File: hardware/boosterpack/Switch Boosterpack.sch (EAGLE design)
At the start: 36 parts, among them IC1 LAUNCHPAD-50MM, Q1 IRFR3709, Q2 IRFR3709, Q3 IRFR3709, Q4 IRFR3709

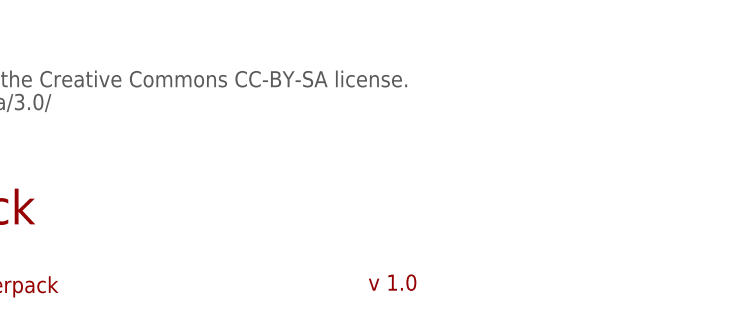
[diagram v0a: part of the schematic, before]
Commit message: Tweaked silkscreen and made OLED ribbon cutoff longer.
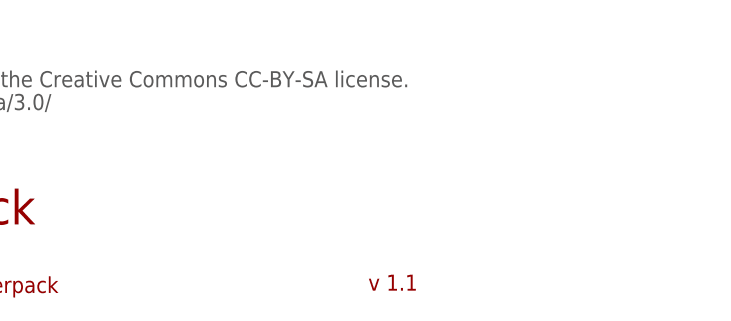
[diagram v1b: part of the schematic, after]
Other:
- note added: "v 1.1"
- note removed: "v 1.0"
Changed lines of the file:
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@@
 <?xml version="1.0" encoding="utf-8"?>
 <!DOCTYPE eagle SYSTEM "eagle.dtd">
-<eagle version="6.2">
+<eagle version="6.3">
 <drawing>
 <settings>
@@
 <layers>
 <layer number="1" name="Top" color="4" fill="1" visible="no" active="no"/>
+<layer number="2" name="Route2" color="1" fill="3" visible="no" active="no"/>
+<layer number="15" name="Route15" color="4" fill="6" visible="no" active="no"/>
 <layer number="16" name="Bottom" color="1" fill="1" visible="no" active="no"/>
 <layer number="17" name="Pads" color="2" fill="1" visible="no" active="no"/>
@@
 <text x="292.1" y="12.7" size="3.81" layer="94">Switch Boosterpack</text>
 <text x="290.83" y="5.08" size="1.778" layer="94">www.github.com/andresv/switch-boosterpack</text>
-<text x="375.412" y="5.334" size="1.778" layer="94">v 1.0</text>
+<text x="375.412" y="5.334" size="1.778" layer="94">v 1.1</text>
 <text x="288.29" y="27.94" size="1.778" layer="97">This work is licensed under version 3.0 of the Creative Commons CC-BY-SA license.</text>
 <text x="288.29" y="25.4" size="1.778" layer="97">http://creativecommons.org/licenses/by-sa/3.0/</text>

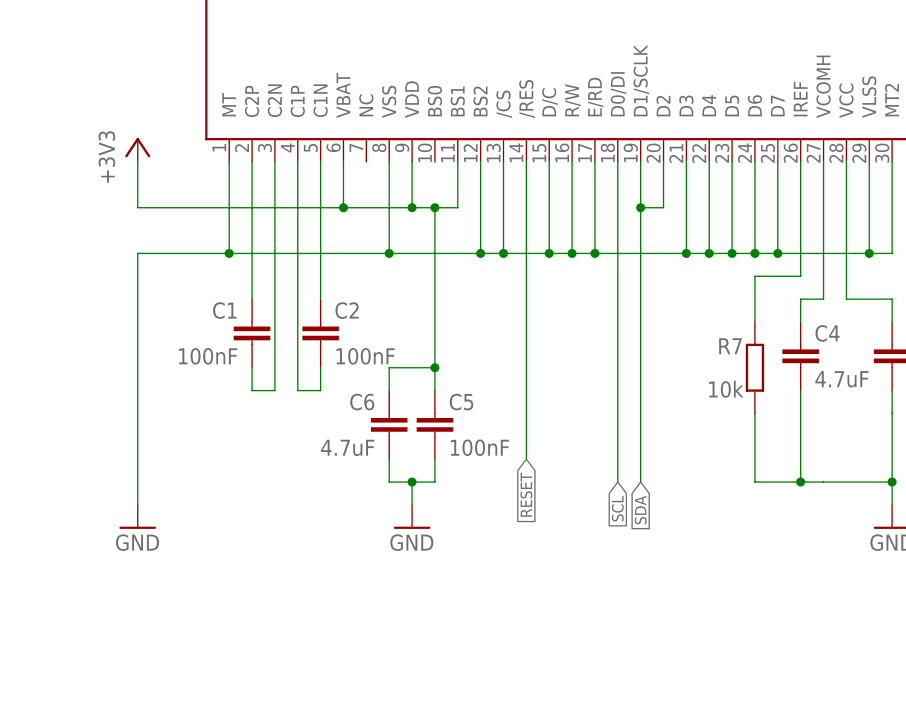
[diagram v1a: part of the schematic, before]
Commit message: BS0 is now tied to GND, C1, C2 are 1 uF and R7 is 390k.
Those are main v1.0 errors. They must be fixed otherwise v1.0 boards are not working.
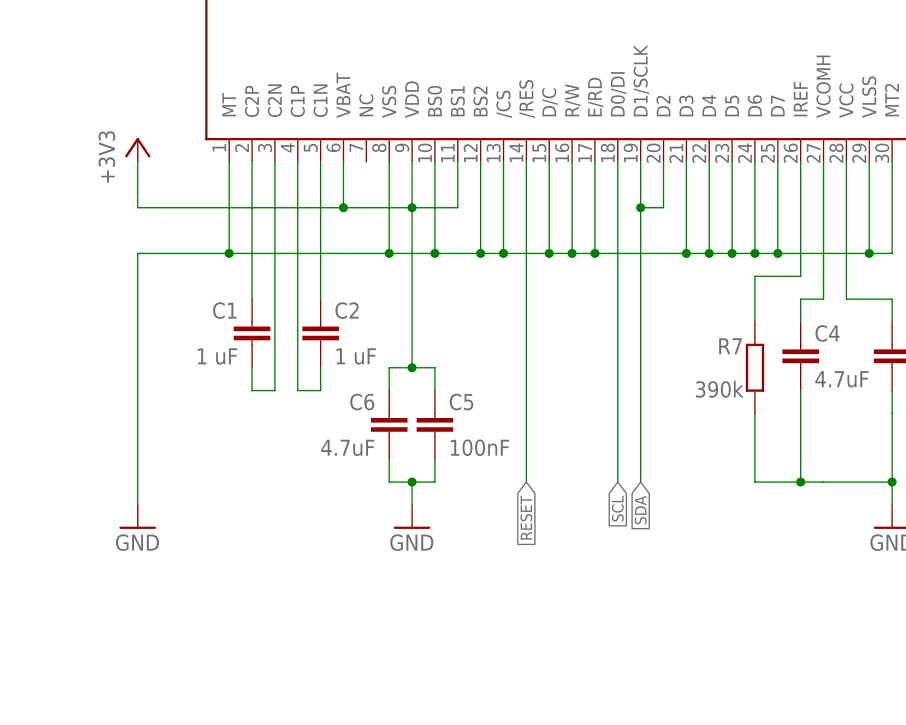
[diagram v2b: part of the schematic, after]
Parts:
- C1, C2: value 100nF -> 1 uF
- R7: value 10k -> 390k
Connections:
- net GND: now also IC3.BS0
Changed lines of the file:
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@@
 <setting verticaltext="up"/>
 </settings>
-<grid distance="0.1" unitdist="inch" unit="inch" style="lines" multiple="1" display="no" altdistance="0.01" altunitdist="inch" altunit="inch"/>
+<grid distance="0.1" unitdist="inch" unit="inch" style="lines" multiple="1" display="yes" altdistance="0.01" altunitdist="inch" altunit="inch"/>
 <layers>
 <layer number="1" name="Top" color="4" fill="1" visible="no" active="no"/>
@@
 <part name="P+5" library="supply1" deviceset="+24V" device=""/>
 <part name="GND5" library="supply1" deviceset="GND" device=""/>
-<part name="C1" library="rcl" deviceset="C-EU" device="C0603" value="100nF"/>
-<part name="C2" library="rcl" deviceset="C-EU" device="C0603" value="100nF"/>
+<part name="C1" library="rcl" deviceset="C-EU" device="C0603" value="1 uF"/>
+<part name="C2" library="rcl" deviceset="C-EU" device="C0603" value="1 uF"/>
 <part name="+3V1" library="supply1" deviceset="+3V3" device=""/>
 <part name="+3V2" library="supply1" deviceset="+3V3" device=""/>
@@
 <part name="GND6" library="supply1" deviceset="GND" device=""/>
 <part name="C4" library="rcl" deviceset="C-EU" device="C0603" value="4.7uF"/>
-<part name="R7" library="rcl" deviceset="R-EU_" device="R0603" value="10k"/>
+<part name="R7" library="rcl" deviceset="R-EU_" device="R0603" value="390k"/>
 <part name="C5" library="rcl" deviceset="C-EU" device="C0603" value="100nF"/>
 <part name="C6" library="rcl" deviceset="C-EU" device="C0603" value="4.7uF"/>
@@
 <pinref part="IC3" gate="G$1" pin="BS2"/>
 <wire x1="68.58" y1="86.36" x2="68.58" y2="76.2" width="0.1524" layer="91"/>
-<wire x1="68.58" y1="76.2" x2="58.42" y2="76.2" width="0.1524" layer="91"/>
+<wire x1="68.58" y1="76.2" x2="63.5" y2="76.2" width="0.1524" layer="91"/>
 <junction x="58.42" y="76.2"/>
 <pinref part="IC3" gate="G$1" pin="/CS"/>
+<wire x1="63.5" y1="76.2" x2="58.42" y2="76.2" width="0.1524" layer="91"/>
 <wire x1="71.12" y1="86.36" x2="71.12" y2="76.2" width="0.1524" layer="91"/>
 <wire x1="71.12" y1="76.2" x2="68.58" y2="76.2" width="0.1524" layer="91"/>
@@
 <wire x1="30.48" y1="76.2" x2="40.64" y2="76.2" width="0.1524" layer="91"/>
 <junction x="40.64" y="76.2"/>
+<pinref part="IC3" gate="G$1" pin="BS0"/>
+<wire x1="63.5" y1="86.36" x2="63.5" y2="76.2" width="0.1524" layer="91"/>
+<junction x="63.5" y="76.2"/>
 </segment>
 <segment>
@@
 <wire x1="53.34" y1="81.28" x2="60.96" y2="81.28" width="0.1524" layer="91"/>
 <pinref part="IC3" gate="G$1" pin="BS1"/>
-<wire x1="60.96" y1="81.28" x2="63.5" y2="81.28" width="0.1524" layer="91"/>
-<wire x1="63.5" y1="81.28" x2="66.04" y2="81.28" width="0.1524" layer="91"/>
+<wire x1="60.96" y1="81.28" x2="66.04" y2="81.28" width="0.1524" layer="91"/>
 <wire x1="66.04" y1="81.28" x2="66.04" y2="86.36" width="0.1524" layer="91"/>
 <wire x1="30.48" y1="81.28" x2="53.34" y2="81.28" width="0.1524" layer="91"/>
@@
 <pinref part="C5" gate="G$1" pin="1"/>
 <wire x1="63.5" y1="60.96" x2="63.5" y2="63.5" width="0.1524" layer="91"/>
-<junction x="63.5" y="81.28"/>
+<wire x1="60.96" y1="63.5" x2="63.5" y2="63.5" width="0.1524" layer="91"/>
 <pinref part="C6" gate="G$1" pin="1"/>
-<wire x1="63.5" y1="63.5" x2="63.5" y2="81.28" width="0.1524" layer="91"/>
 <wire x1="58.42" y1="60.96" x2="58.42" y2="63.5" width="0.1524" layer="91"/>
-<wire x1="58.42" y1="63.5" x2="63.5" y2="63.5" width="0.1524" layer="91"/>
-<junction x="63.5" y="63.5"/>
+<wire x1="58.42" y1="63.5" x2="60.96" y2="63.5" width="0.1524" layer="91"/>
+<wire x1="60.96" y1="81.28" x2="60.96" y2="63.5" width="0.1524" layer="91"/>
+<junction x="60.96" y="63.5"/>
 </segment>
 <segment>
@@
 <segment>
 <pinref part="IC3" gate="G$1" pin="/RES"/>
-<wire x1="73.66" y1="86.36" x2="73.66" y2="53.34" width="0.1524" layer="91"/>
-<label x="73.66" y="53.34" size="1.27" layer="95" rot="R270" xref="yes"/>
-</segment>
-<segment>
+<wire x1="73.66" y1="86.36" x2="73.66" y2="50.8" width="0.1524" layer="91"/>
+<label x="73.66" y="50.8" size="1.27" layer="95" rot="R270" xref="yes"/>
+</segment>
+<segment>

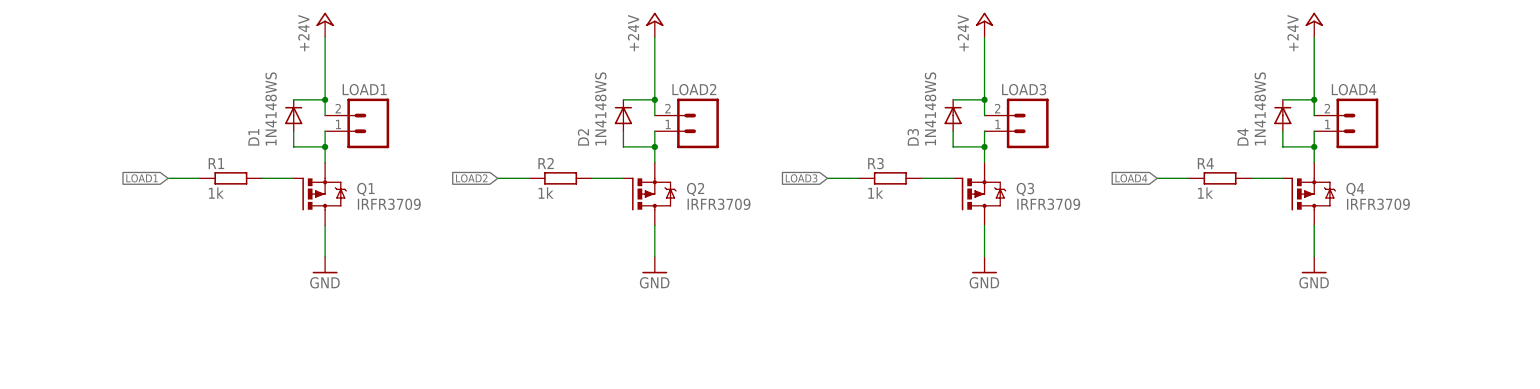
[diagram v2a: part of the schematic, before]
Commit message: Fixed schematic, instead of N channel FET there were P channel FET on schematic.
So actually 1.0 board MOSFET side was messed up. Now it is correct. P channel FET was used in "N channel configuration".
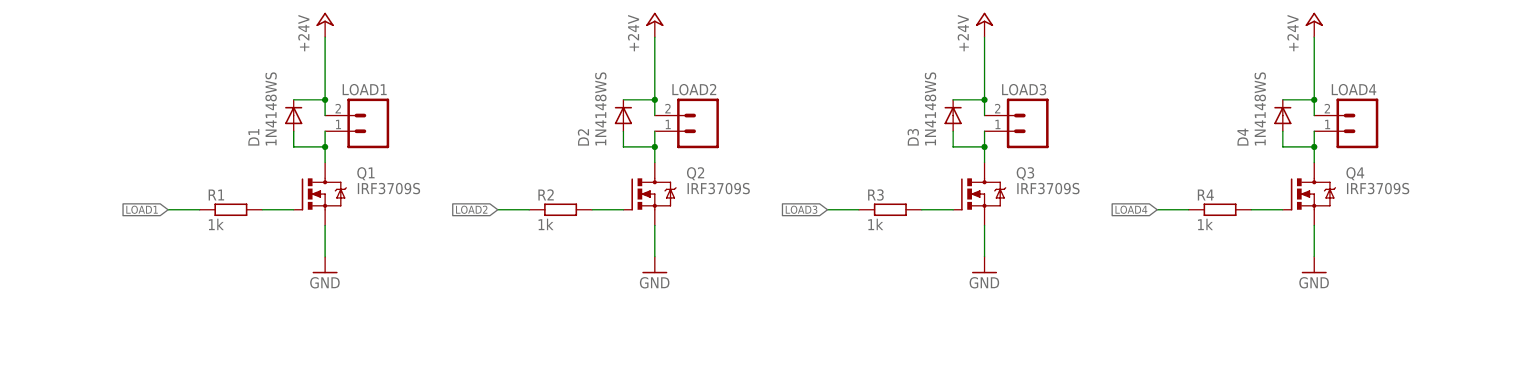
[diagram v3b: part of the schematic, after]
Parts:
- Q1, Q2, Q3, Q4: value IRFR3709 -> IRF3709S; device transistor-power:IRFR5305 -> mosfet:IRFR3709
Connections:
- net GND: now also Q1.S, Q2.S, Q3.S, Q4.S; no longer Q1.D, Q2.D, Q3.D, Q4.D
- net N$1: now also Q1.D; no longer Q1.S
- net N$3: now also Q2.D; no longer Q2.S
- net N$5: now also Q3.D; no longer Q3.S
- net N$7: now also Q4.D; no longer Q4.S
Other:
- moved on the sheet: R1, R2, R3, R4
